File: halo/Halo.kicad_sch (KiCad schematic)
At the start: 79 parts, among them J1 USB-C 16P, J2 5V / GND alt, Q1 ALS-PT19-315C, SW1 RESET, SW2 BOOT, SW3 USER, U1 ESP32-C3-MINI-1-N4, U2 AMS1117-3.3, U3 74AHCT1G125

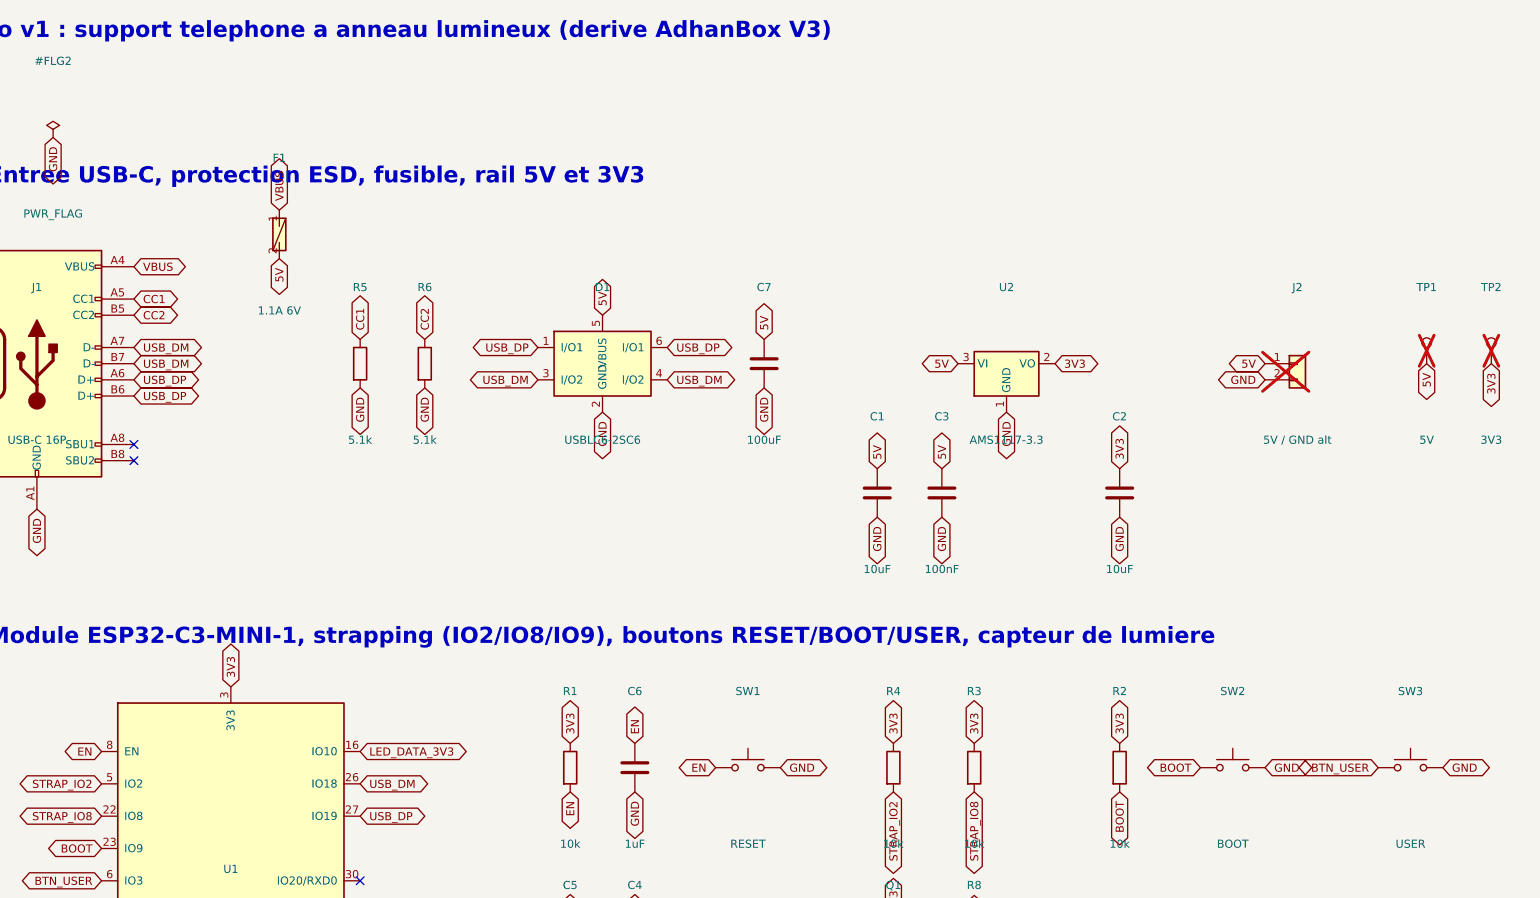
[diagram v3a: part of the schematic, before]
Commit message: Halo v2 : schema de la chaine d'alimentation 9 V, ERC a zero
- U4 CH224A demande 9 V au chargeur PD (Rset 6.8k sur CFG1) ; DP/DM restent a
  l'ESP32 pour le flashage, PG inutilise. Le bus apres fusible devient VBUS_F.
- U5 MT2492 + L1 4.7 uH font le 5 V des LEDs (100k / 13.7k -> 4.98 V, EN par
  pont 100k/100k car EN est limite a 6 V). U2 devient un AP2112K-3.3 a faible
  chute. F1 passe en PTC 1812 16 V 2.5 A. J3 : deux trous pour le module Qi.
  R5/R6 (5.1k sur CC) disparaissent. D1 reste reference au 5 V (9 V interdit).
- Correction au passage : la description du symbole WS2812B contenait un \n
  litteral depuis le 09/09, KiCad refusait de charger le schema ; l'ERC
  n'avait pas ete rejoue apres ce changement.
- BOM : lignes v2 avec codes LCSC verifies en stock ; HALO_V2.md et SCHEMA.md.

Le PCB ne connait pas encore ces pieces : gen_kicad_pcb.py est l'etape suivante.

Co-Authored-By: Claude Fable 5.1 <noreply@anthropic.com>
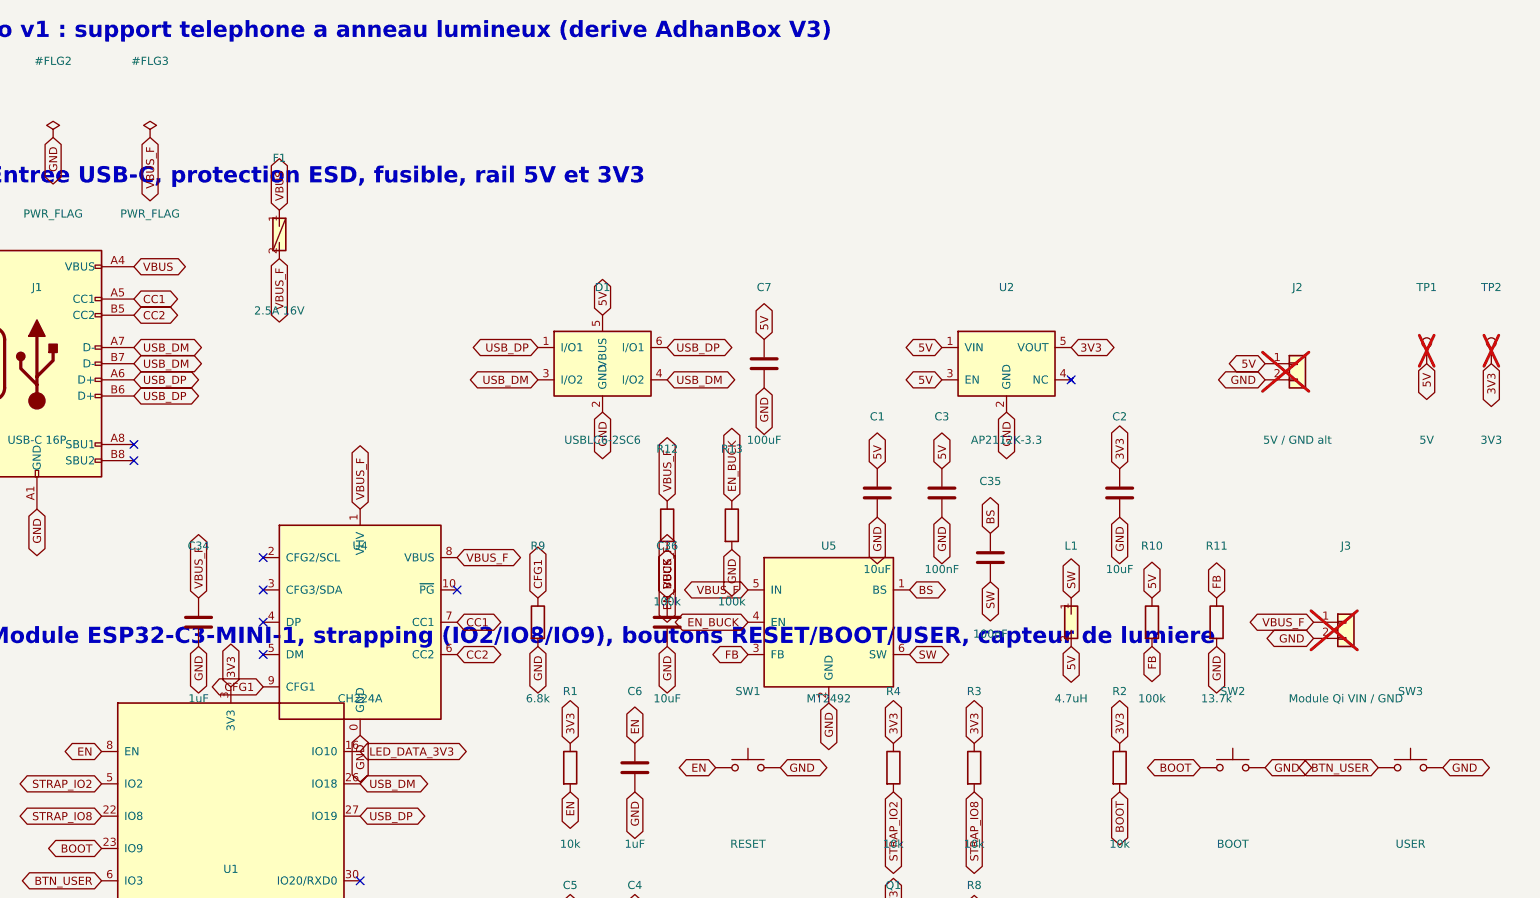
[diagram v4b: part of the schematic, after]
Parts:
- removed R5, R6: 5.1k, Resistor_SMD:R_0805_2012Metric, symbol Device:R
- added C34: 1uF, Capacitor_SMD:C_0805_2012Metric, symbol Device:C
- added C35: 100nF, Capacitor_SMD:C_0805_2012Metric, symbol Device:C
- added C36: 10uF, Capacitor_SMD:C_0805_2012Metric, symbol Device:C
- added J3: Module Qi VIN / GND, Connector_PinHeader_2.54mm:PinHeader_1x02_P2.54mm_Vertical, symbol Connector_Generic:Conn_01x02
- added L1: 4.7uH, Inductor_SMD:L_Taiyo-Yuden_NR-50xx, symbol Halo:L
- added R10, R12, R13: 100k, Resistor_SMD:R_0805_2012Metric, symbol Device:R
- added R11: 13.7k, Resistor_SMD:R_0805_2012Metric, symbol Device:R
- added R9: 6.8k, Resistor_SMD:R_0805_2012Metric, symbol Device:R
- added U4: CH224A, Package_SO:SSOP-10_3.9x4.9mm_P1.00mm, symbol Halo:CH224A
- added U5: MT2492, Package_TO_SOT_SMD:SOT-23-6, symbol Halo:MT2492
- F1: value 1.1A 6V -> 2.5A 16V; footprint Fuse:Fuse_1206_3216Metric -> Fuse:Fuse_1812_4532Metric
- U2: value AMS1117-3.3 -> AP2112K-3.3; footprint Package_TO_SOT_SMD:SOT-223-3_TabPin2 -> Package_TO_SOT_SMD:SOT-23-5; symbol Halo:AMS1117-3.3 -> Halo:AP2112K
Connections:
- net 3V3: now also U2.5 (VOUT); no longer U2.2 (VO)
- net 5V: now also U2.1 (VIN), L1.2, R10.1; no longer F1.2
- net CC1: now also U4.7 (CC1)
- net CC2: now also U4.6 (CC2)
- net GND: now also U2.2 (GND), C34.2, C36.2, J3.2 (Pin_2), R11.2, R13.2, R9.2, U4.0 (GND), U5.2 (GND); no longer U2.1 (GND)
- new net BS: C35.1, U5.1 (BS)
- new net CFG1: R9.1, U4.9 (CFG1)
- new net EN_BUCK: R12.2, R13.1, U5.4 (EN)
- new net FB: R10.2, R11.1, U5.3 (FB)
- new net SW: C35.2, L1.1, U5.6 (SW)
- new net VBUS_F: C34.1, C36.1, F1.2, J3.1 (Pin_1), R12.1, U4.1 (VHV), U4.8 (VBUS), U5.5 (IN)
- no-connect marks 10 -> 16
